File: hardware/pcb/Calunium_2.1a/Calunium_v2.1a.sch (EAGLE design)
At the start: 65 parts, among them IC1 MCP1702-3.3, IC2 DS1338, IC3 MCP1702-5.0, IC4 ATMEGA1284, IC5 MCP2200, Q1 2N7000, U1 CALUNIUM-SHIELD, X1 PWR, X2 JTAG, X3 USB, X4 CONN-SMATHD, X5 UART0, X6 MICRO-SD-SOCKETHIROSE-DM3D, Y1 32k768, Y2 16MHz, Y3 12MHz

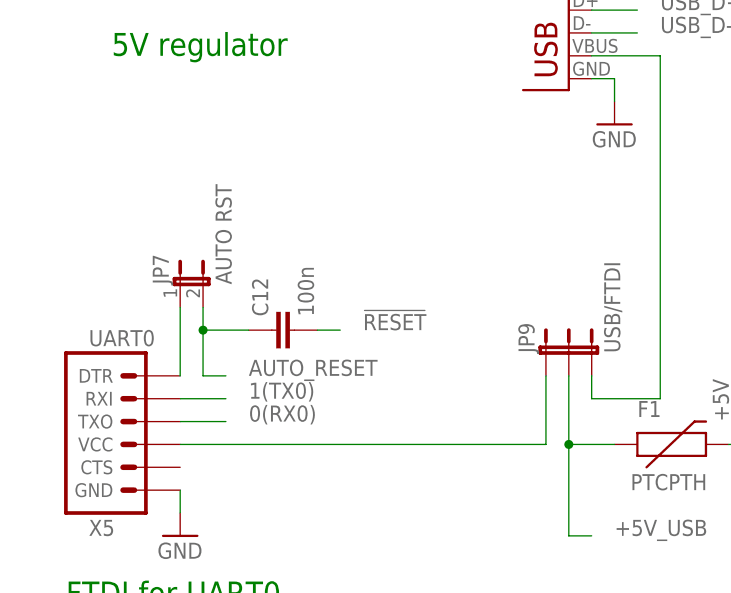
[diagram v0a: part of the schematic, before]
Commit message: Fixing error where MCP2200 autoreset was not routed through JP7.
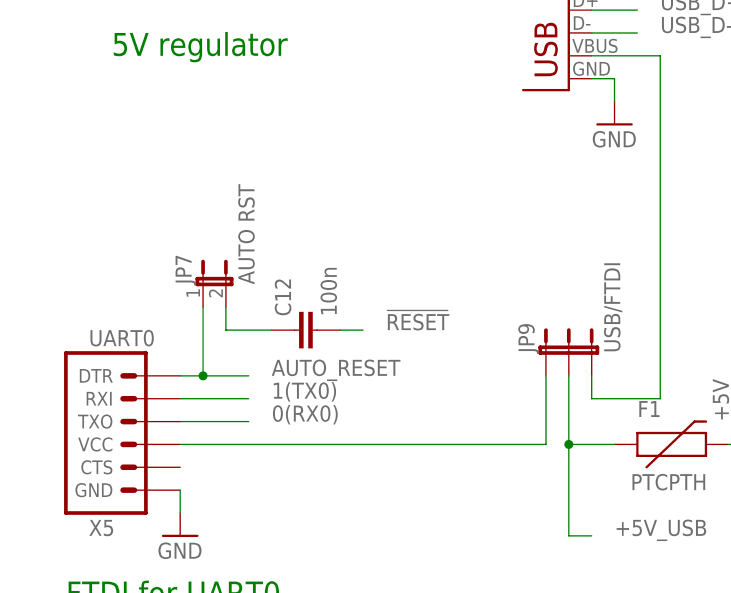
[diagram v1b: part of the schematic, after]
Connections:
- net AUTO_RESET: now also JP7.1, X5.DTR; no longer C12.1, JP7.2
- net N$15: now also C12.1, JP7.2; no longer JP7.1, X5.DTR
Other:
- moved on the sheet: C12, JP7
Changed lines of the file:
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@@
 <?xml version="1.0" encoding="utf-8"?>
 <!DOCTYPE eagle SYSTEM "eagle.dtd">
-<eagle version="6.2">
+<eagle version="6.5.0">
 <drawing>
 <settings>
@@
 <instance part="R6" gate="G$1" x="-149.86" y="68.58" rot="R90"/>
 <instance part="SENS1" gate="G$1" x="157.48" y="27.94" rot="MR0"/>
-<instance part="JP7" gate="A" x="-144.78" y="-25.4"/>
-<instance part="C12" gate="G$1" x="-132.08" y="-30.48" rot="R90"/>
+<instance part="JP7" gate="A" x="-142.24" y="-25.4"/>
+<instance part="C12" gate="G$1" x="-129.54" y="-30.48" rot="R90"/>
 <instance part="R3" gate="G$1" x="170.18" y="78.74" rot="R90"/>
 <instance part="R4" gate="G$1" x="177.8" y="78.74" rot="R90"/>
@@
 </segment>
 <segment>
-<wire x1="-129.54" y1="-30.48" x2="-127" y2="-30.48" width="0.1524" layer="91"/>
-<label x="-124.46" y="-30.48" size="1.778" layer="95"/>
+<wire x1="-127" y1="-30.48" x2="-124.46" y2="-30.48" width="0.1524" layer="91"/>
+<label x="-121.92" y="-30.48" size="1.778" layer="95"/>
 <pinref part="C12" gate="G$1" pin="2"/>
 </segment>
@@
 </segment>
 <segment>
-<wire x1="-144.78" y1="-38.1" x2="-139.7" y2="-38.1" width="0.1524" layer="91"/>
-<label x="-137.16" y="-38.1" size="1.778" layer="95"/>
+<wire x1="-144.78" y1="-38.1" x2="-137.16" y2="-38.1" width="0.1524" layer="91"/>
+<label x="-134.62" y="-38.1" size="1.778" layer="95"/>
 <pinref part="X5" gate="G$1" pin="RXI"/>
 </segment>
@@
 </segment>
 <segment>
-<wire x1="-144.78" y1="-40.64" x2="-139.7" y2="-40.64" width="0.1524" layer="91"/>
-<label x="-137.16" y="-40.64" size="1.778" layer="95"/>
+<wire x1="-144.78" y1="-40.64" x2="-137.16" y2="-40.64" width="0.1524" layer="91"/>
+<label x="-134.62" y="-40.64" size="1.778" layer="95"/>
 <pinref part="X5" gate="G$1" pin="TXO"/>
 </segment>
@@
 </segment>
 </net>
-<net name="N$15" class="0">
-<segment>
-<wire x1="-144.78" y1="-35.56" x2="-144.78" y2="-27.94" width="0.1524" layer="91"/>
+<net name="AUTO_RESET" class="0">
+<segment>
+<label x="-134.62" y="-35.56" size="1.778" layer="95"/>
+<wire x1="-144.78" y1="-35.56" x2="-142.24" y2="-35.56" width="0.1524" layer="91"/>
+<wire x1="-142.24" y1="-35.56" x2="-142.24" y2="-27.94" width="0.1524" layer="91"/>
 <pinref part="X5" gate="G$1" pin="DTR"/>
 <pinref part="JP7" gate="A" pin="1"/>
-</segment>
-</net>
-<net name="AUTO_RESET" class="0">
-<segment>
-<wire x1="-142.24" y1="-27.94" x2="-142.24" y2="-30.48" width="0.1524" layer="91"/>
-<pinref part="JP7" gate="A" pin="2"/>
-<pinref part="C12" gate="G$1" pin="1"/>
-<junction x="-142.24" y="-30.48"/>
-<wire x1="-142.24" y1="-30.48" x2="-137.16" y2="-30.48" width="0.1524" layer="91"/>
-<wire x1="-142.24" y1="-30.48" x2="-142.24" y2="-35.56" width="0.1524" layer="91"/>
-<wire x1="-142.24" y1="-35.56" x2="-139.7" y2="-35.56" width="0.1524" layer="91"/>
-<label x="-137.16" y="-35.56" size="1.778" layer="95"/>
+<junction x="-142.24" y="-35.56"/>
+<wire x1="-142.24" y1="-35.56" x2="-137.16" y2="-35.56" width="0.1524" layer="91"/>
 </segment>
 <segment>
@@
 </segment>
 </net>
+<net name="N$15" class="0">
+<segment>
+<pinref part="C12" gate="G$1" pin="1"/>
+<pinref part="JP7" gate="A" pin="2"/>
+<wire x1="-139.7" y1="-27.94" x2="-139.7" y2="-30.48" width="0.1524" layer="91"/>
+<wire x1="-139.7" y1="-30.48" x2="-134.62" y2="-30.48" width="0.1524" layer="91"/>
+</segment>
+</net>

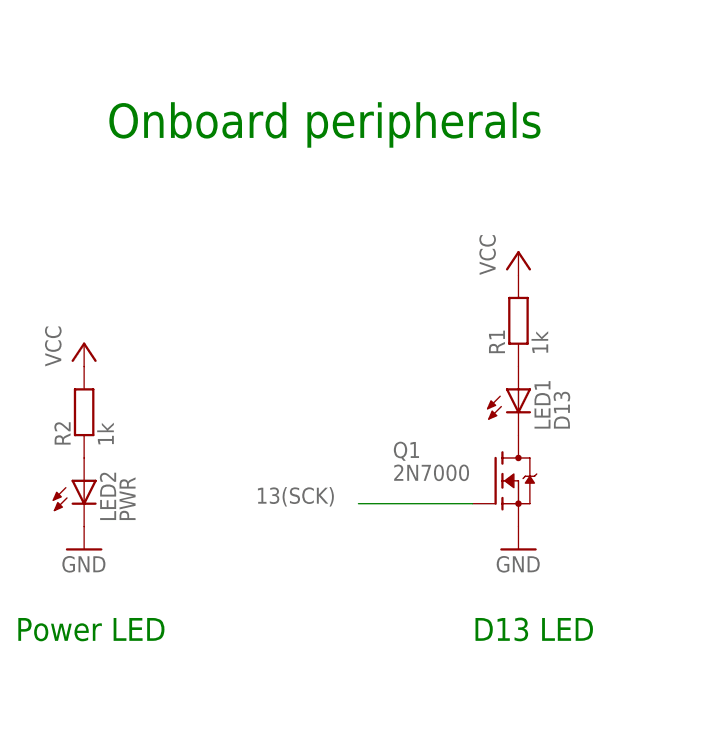
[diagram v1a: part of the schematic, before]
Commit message: Adding 1M pull-down resistor on D13.
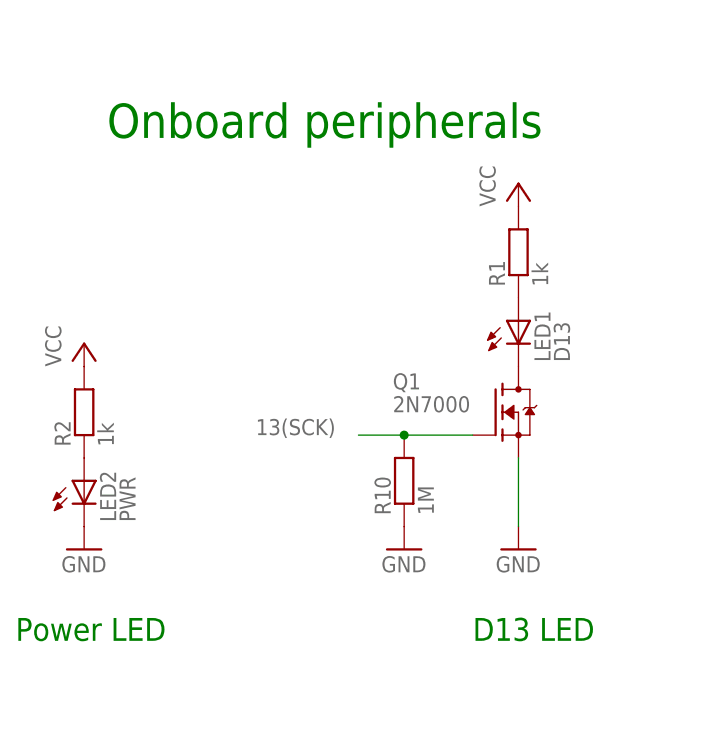
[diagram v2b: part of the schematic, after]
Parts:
- added R10: 1M, SteveMarple:RESISTOR
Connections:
- net 13(SCK): now also R10.2
- net GND: now also R10.1
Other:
- moved on the sheet: LED1, Q1, R1
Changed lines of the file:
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@@
 <?xml version="1.0" encoding="utf-8"?>
 <!DOCTYPE eagle SYSTEM "eagle.dtd">
-<eagle version="6.5.0">
+<eagle version="6.4">
 <drawing>
 <settings>
@@
 <part name="GND29" library="supply1" deviceset="GND" device=""/>
 <part name="GND30" library="supply1" deviceset="GND" device=""/>
+<part name="R10" library="SteveMarple" deviceset="RESISTOR" device="" value="1M"/>
+<part name="GND31" library="supply1" deviceset="GND" device=""/>
 </parts>
 <sheets>
@@
 <instance part="X3" gate="G$1" x="-101.6" y="-2.54" smashed="yes" rot="MR0"/>
 <instance part="X5" gate="G$1" x="-149.86" y="-40.64" rot="MR180"/>
-<instance part="Q1" gate="G$1" x="185.42" y="124.46"/>
+<instance part="Q1" gate="G$1" x="185.42" y="132.08"/>
 <instance part="U1" gate="G$1" x="48.26" y="106.68"/>
 <instance part="IC2" gate="G$1" x="142.24" y="66.04"/>
-<instance part="LED1" gate="G$1" x="185.42" y="134.62"/>
+<instance part="LED1" gate="G$1" x="185.42" y="142.24"/>
 <instance part="LED2" gate="G$1" x="137.16" y="124.46"/>
-<instance part="R1" gate="G$1" x="185.42" y="142.24" rot="R90"/>
+<instance part="R1" gate="G$1" x="185.42" y="149.86" rot="R90"/>
 <instance part="Y1" gate="G$1" x="114.3" y="86.36" smashed="yes" rot="R180">
 <attribute name="NAME" x="111.76" y="92.456" size="1.778" layer="95"/>
@@
 <instance part="H4" gate="G$1" x="106.68" y="-63.5"/>
 <instance part="GND2" gate="1" x="88.9" y="-60.96"/>
-<instance part="P+7" gate="VCC" x="185.42" y="149.86"/>
+<instance part="P+7" gate="VCC" x="185.42" y="157.48"/>
 <instance part="P+10" gate="VCC" x="137.16" y="139.7"/>
 <instance part="GND4" gate="1" x="137.16" y="116.84"/>
@@
 <instance part="GND29" gate="1" x="119.38" y="73.66"/>
 <instance part="GND30" gate="1" x="109.22" y="73.66"/>
+<instance part="R10" gate="G$1" x="172.72" y="124.46" rot="R90"/>
+<instance part="GND31" gate="1" x="172.72" y="116.84"/>
 </instances>
 <busses>
@@
 <pinref part="Q1" gate="G$1" pin="S"/>
 <pinref part="GND3" gate="1" pin="GND"/>
+<wire x1="185.42" y1="127" x2="185.42" y2="119.38" width="0.1524" layer="91"/>
 </segment>
 <segment>
@@
 <pinref part="C18" gate="G$1" pin="2"/>
 <pinref part="GND30" gate="1" pin="GND"/>
+</segment>
+<segment>
+<pinref part="R10" gate="G$1" pin="1"/>
+<pinref part="GND31" gate="1" pin="GND"/>
 </segment>
 </net>
@@
 <segment>
 <pinref part="Q1" gate="G$1" pin="G"/>
-<wire x1="180.34" y1="121.92" x2="167.64" y2="121.92" width="0.1524" layer="91"/>
-<label x="165.1" y="121.92" size="1.778" layer="95" rot="MR0"/>
-</segment>
-<segment>
+<wire x1="180.34" y1="129.54" x2="172.72" y2="129.54" width="0.1524" layer="91"/>
+<label x="165.1" y="129.54" size="1.778" layer="95" rot="MR0"/>
+<pinref part="R10" gate="G$1" pin="2"/>
+<wire x1="172.72" y1="129.54" x2="167.64" y2="129.54" width="0.1524" layer="91"/>
+<junction x="172.72" y="129.54"/>
+</segment>
+<segment>

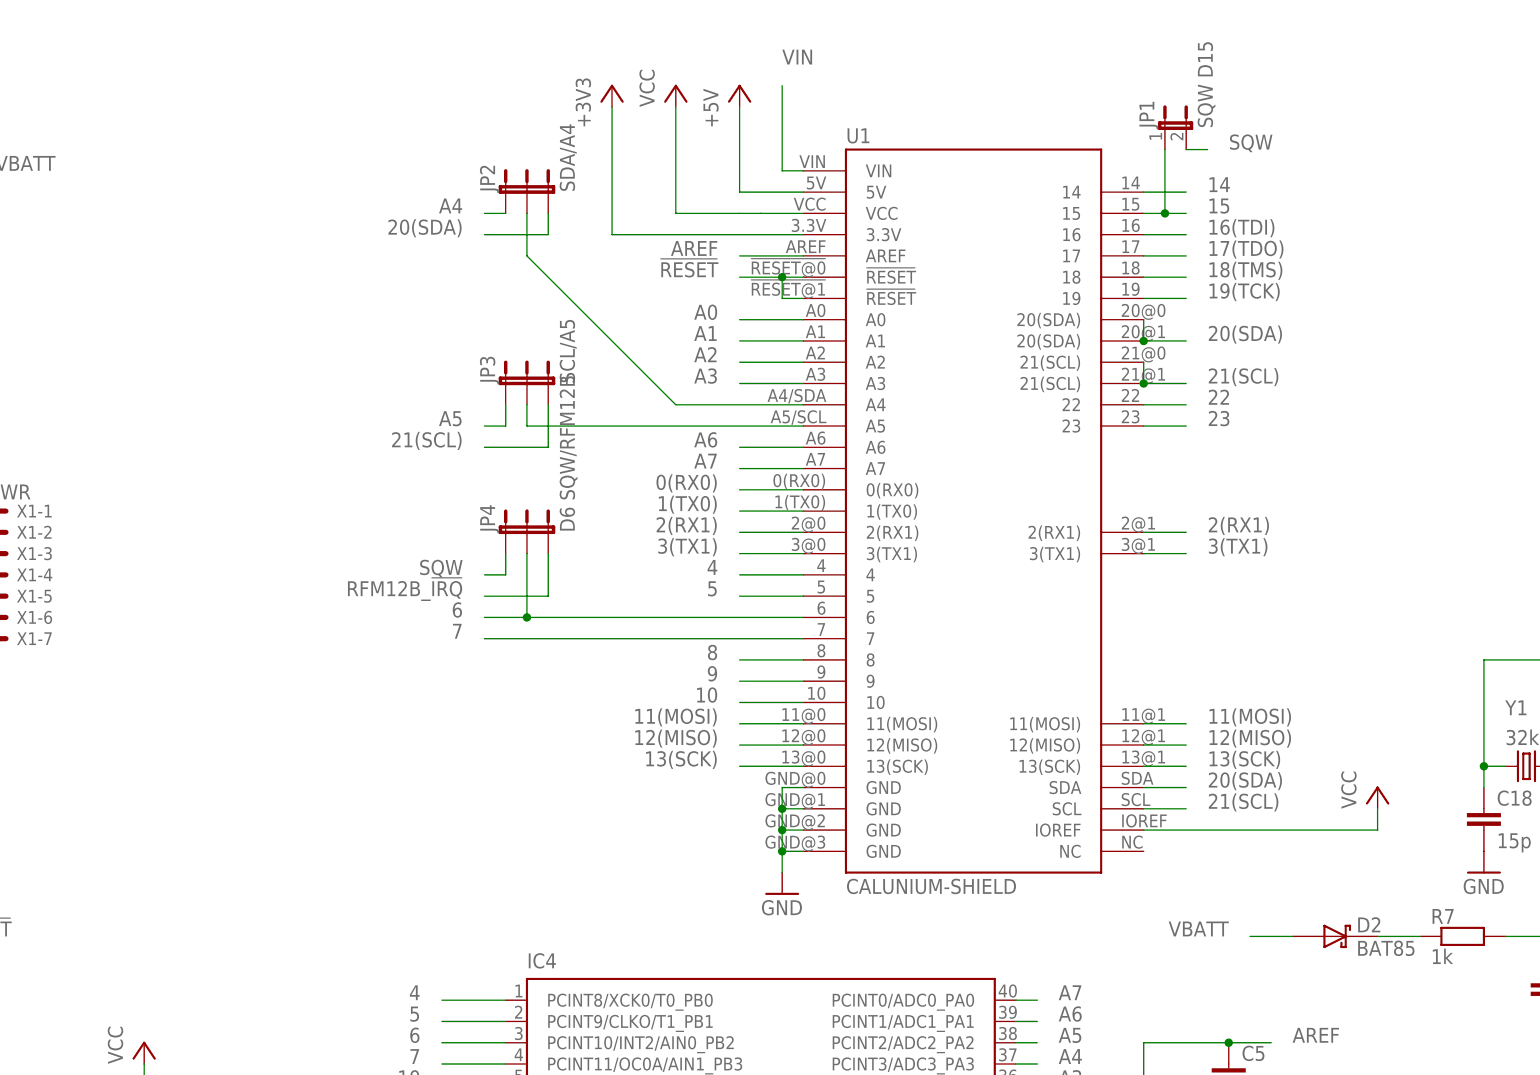
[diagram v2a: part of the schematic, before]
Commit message: Adding juumper to disconnect VCC from ISP header, routing improvements.
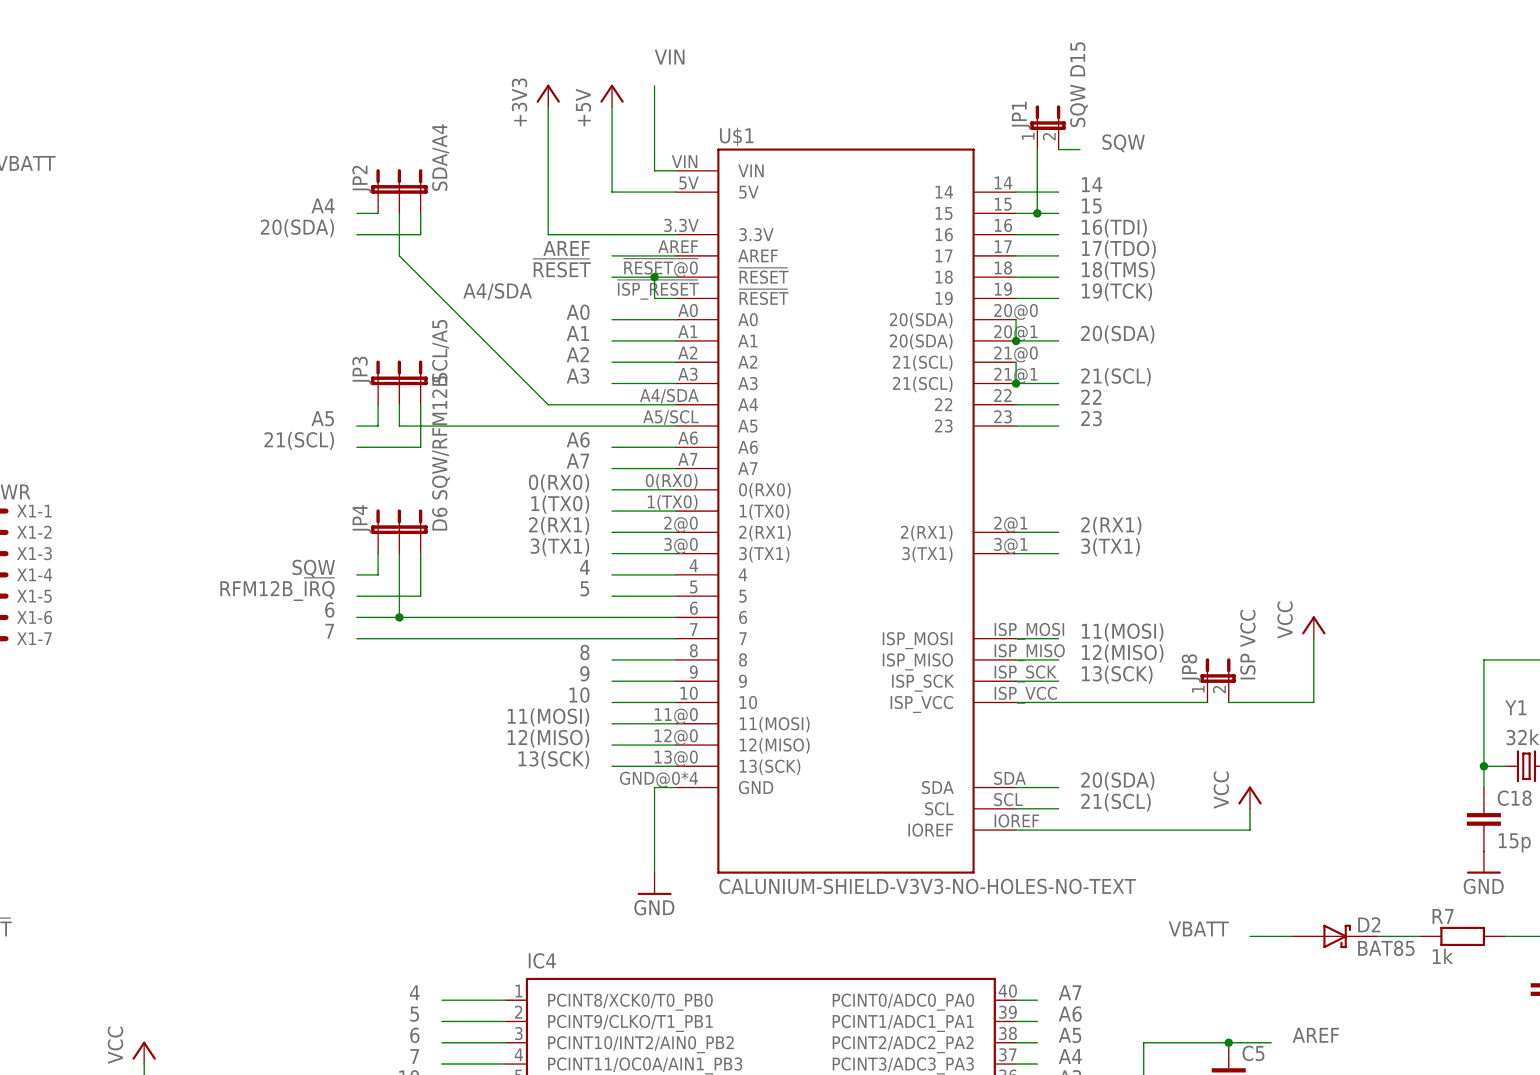
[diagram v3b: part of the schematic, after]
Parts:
- removed U1: CALUNIUM-SHIELD, SteveMarple:CALUNIUM-SHIELD-V2NO-OUTLINE-NO-HOLES-NO-TEXT
- added JP8: ISP VCC, SparkFun:JUMPER-2PTH
- added U$1: CALUNIUM-SHIELD-V3V3-NO-HOLES-NO-TEXT, SteveMarple:CALUNIUM-SHIELD-V3V3-NO-HOLES-NO-TEXT
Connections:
- removed net N$13: JP3.2, U1.A5
- new net A4/SDA: JP2.2, U$1.A4
- new net A5/SCL: JP3.2, U$1.A5
- net !RESET: now also U$1.!RESET@0, U$1.!RESET@1; no longer U1.!RESET@0, U1.!RESET@1
- net +3V3: now also U$1.3.3V; no longer U1.3.3V
- net +5V: now also U$1.5V; no longer U1.5V
- net 0(RX0): now also U$1.0(RX0); no longer U1.0(RX0)
- net 1(TX0): now also U$1.1(TX0); no longer U1.1(TX0)
- net 10: now also U$1.10; no longer U1.10
- net 11(MOSI): now also U$1.11(MOSI), U$1.ISP_MOSI; no longer U1.11(MOSI)@0, U1.11(MOSI)@1
- net 12(MISO): now also U$1.12(MISO), U$1.ISP_MISO; no longer U1.12(MISO)@0, U1.12(MISO)@1
- net 13(SCK): now also U$1.13(SCK), U$1.ISP_SCK; no longer U1.13(SCK)@0, U1.13(SCK)@1
- net 14: now also U$1.14; no longer U1.14
- net 15: now also U$1.15; no longer U1.15
- net 16(TDI): now also U$1.16; no longer U1.16
- net 17(TDO): now also U$1.17; no longer U1.17
- net 18(TMS): now also U$1.18; no longer U1.18
- net 19(TCK): now also U$1.19; no longer U1.19
- net 2(RX1): now also U$1.2(RX1)@0, U$1.2(RX1)@1; no longer U1.2(RX1)@0, U1.2(RX1)@1
- net 20(SDA): now also U$1.20(SDA)@0, U$1.20(SDA)@1, U$1.SDA; no longer U1.20(SDA)@0, U1.20(SDA)@1, U1.SDA
- net 21(SCL): now also U$1.21(SCL)@0, U$1.21(SCL)@1, U$1.SCL; no longer U1.21(SCL)@0, U1.21(SCL)@1, U1.SCL
- net 22: now also U$1.22; no longer U1.22
- net 23: now also U$1.23; no longer U1.23
- net 3(TX1): now also U$1.3(TX1)@0, U$1.3(TX1)@1; no longer U1.3(TX1)@0, U1.3(TX1)@1
- net 4: now also U$1.4; no longer U1.4
- net 5: now also U$1.5; no longer U1.5
- net 6: now also U$1.6; no longer U1.6
- net 7: now also U$1.7; no longer U1.7
- net 8: now also U$1.8; no longer U1.8
- net 9: now also U$1.9; no longer U1.9
- net A0: now also U$1.A0; no longer U1.A0
- net A1: now also U$1.A1; no longer U1.A1
- net A2: now also U$1.A2; no longer U1.A2
- net A3: now also U$1.A3; no longer U1.A3
- net A6: now also U$1.A6; no longer U1.A6
- net A7: now also U$1.A7; no longer U1.A7
- net AREF: now also U$1.AREF; no longer U1.AREF
- net GND: now also U$1.GND; no longer U1.GND@0, U1.GND@1, U1.GND@2, U1.GND@3
- net N$6: now also JP8.1, U$1.ISP_VCC; no longer JP2.2, U1.A4
- net VCC: now also JP8.2, U$1.IOREF; no longer U1.IOREF, U1.VCC
- net VIN: now also U$1.VIN; no longer U1.VIN
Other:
- moved on the sheet: JP1, JP2, JP3, JP4
